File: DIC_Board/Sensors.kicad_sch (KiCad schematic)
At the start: 0 parts

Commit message: Separated the power sheets, did the sensor sheets.
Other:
- added sheet ADMONT K96 (admont_k96.kicad_sch)
- added sheet Licor (Licor.kicad_sch)
- added sheet O2 Sensor (o2_sensor.kicad_sch)
- added sheet RH Sensor (rh_sensor.kicad_sch)
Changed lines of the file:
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@@
 		(title "Sensors")
 	)
+	(sheet
+		(at 55.88 44.45)
+		(size 21.59 24.13)
+		(exclude_from_sim no)
+		(in_bom yes)
+		(on_board yes)
+		(dnp no)
+		(fields_autoplaced yes)
+		(stroke
+			(width 0.1524)
+			(type solid)
+		)
+		(fill
+			(color 0 0 0 0)
+		)
+		(property "Sheetname" "Licor"
+			(at 55.88 43.7384 0)
+			(show_name no)
+			(do_not_autoplace no)
+			(effects
+				(font
+					(size 1.27 1.27)
+				)
+				(justify left bottom)
+			)
+		)
+		(property "Sheetfile" "Licor.kicad_sch"
+			(at 55.88 69.1646 0)
+			(show_name no)
+			(do_not_autoplace no)
+			(effects
+				(font
+					(size 1.27 1.27)
+				)
+				(justify left top)
+			)
+		)
+		(instances
+			(project "DIC_Board"
+				(path "/bb0ef0df-c181-443a-843c-695cd2e0efee/15388a04-aea8-414b-8903-58a719a8054d"
+					(page "13")
+				)
+			)
+		)
+	)
+	(sheet
+		(at 101.6 44.45)
+		(size 30.48 24.13)
+		(exclude_from_sim no)
+		(in_bom yes)
+		(on_board yes)
+		(dnp no)
+		(fields_autoplaced yes)
+		(stroke
+			(width 0.1524)
+			(type solid)
+		)
+		(fill
+			(color 0 0 0 0)
+		)
+		(property "Sheetname" "RH Sensor"
+			(at 101.6 43.7384 0)
+			(show_name no)
+			(do_not_autoplace no)
+			(effects
+				(font
+					(size 1.27 1.27)
+				)
+				(justify left bottom)
+			)
+		)
+		(property "Sheetfile" "rh_sensor.kicad_sch"
+			(at 101.6 69.1646 0)
+			(show_name no)
+			(do_not_autoplace no)
+			(effects
+				(font
+					(size 1.27 1.27)
+				)
+				(justify left top)
+			)
+		)
+		(instances
+			(project "DIC_Board"
+				(path "/bb0ef0df-c181-443a-843c-695cd2e0efee/15388a04-aea8-414b-8903-58a719a8054d"
+					(page "14")
+				)
+			)
+		)
+	)
+	(sheet
+		(at 151.13 44.45)
+		(size 25.4 25.4)
+		(exclude_from_sim no)
+		(in_bom yes)
+		(on_board yes)
+		(dnp no)
+		(fields_autoplaced yes)
+		(stroke
+			(width 0.1524)
+			(type solid)
+		)
+		(fill
+			(color 0 0 0 0)
+		)
+		(property "Sheetname" "O2 Sensor"
+			(at 151.13 43.7384 0)
+			(show_name no)
+			(do_not_autoplace no)
+			(effects
+				(font
+					(size 1.27 1.27)
+				)
+				(justify left bottom)
+			)
+		)
+		(property "Sheetfile" "o2_sensor.kicad_sch"
+			(at 151.13 70.4346 0)
+			(show_name no)
+			(do_not_autoplace no)
+			(effects
+				(font
+					(size 1.27 1.27)
+				)
+				(justify left top)
+			)
+		)
+		(instances
+			(project "DIC_Board"
+				(path "/bb0ef0df-c181-443a-843c-695cd2e0efee/15388a04-aea8-414b-8903-58a719a8054d"
+					(page "15")
+				)
+			)
+		)
+	)
+	(sheet
+		(at 191.77 46.99)
+		(size 26.67 24.13)
+		(exclude_from_sim no)
+		(in_bom yes)
+		(on_board yes)
+		(dnp no)
+		(fields_autoplaced yes)
+		(stroke
+			(width 0.1524)
+			(type solid)
+		)
+		(fill
+			(color 0 0 0 0)
+		)
+		(property "Sheetname" "ADMONT K96"
+			(at 191.77 46.2784 0)
+			(show_name no)
+			(do_not_autoplace no)
+			(effects
+				(font
+					(size 1.27 1.27)
+				)
+				(justify left bottom)
+			)
+		)
+		(property "Sheetfile" "admont_k96.kicad_sch"
+			(at 191.77 71.7046 0)
+			(show_name no)
+			(do_not_autoplace no)
+			(effects
+				(font
+					(size 1.27 1.27)
+				)
+				(justify left top)
+			)
+		)
+		(instances
+			(project "DIC_Board"
+				(path "/bb0ef0df-c181-443a-843c-695cd2e0efee/15388a04-aea8-414b-8903-58a719a8054d"
+					(page "16")
+				)
+			)
+		)
+	)
 )

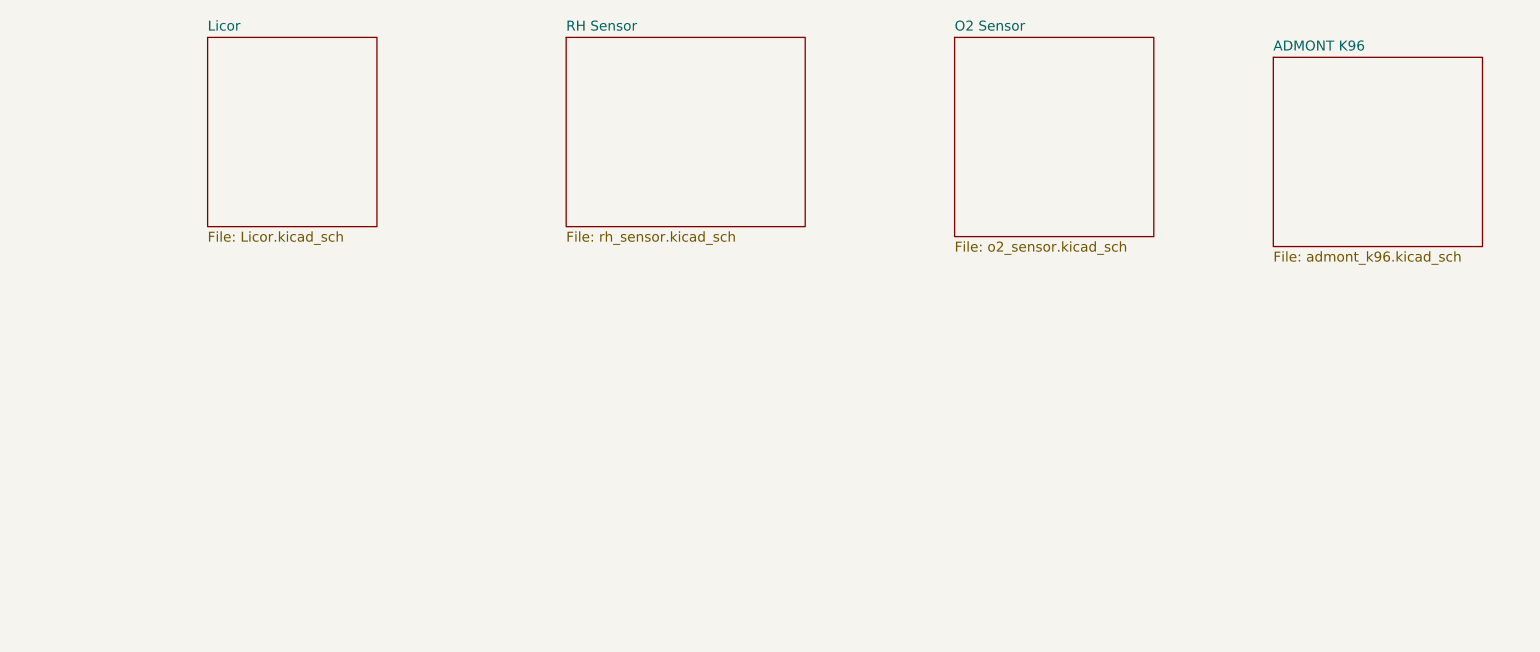
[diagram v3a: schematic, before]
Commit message: Synchronize schematic hierarchy and MCU pin map
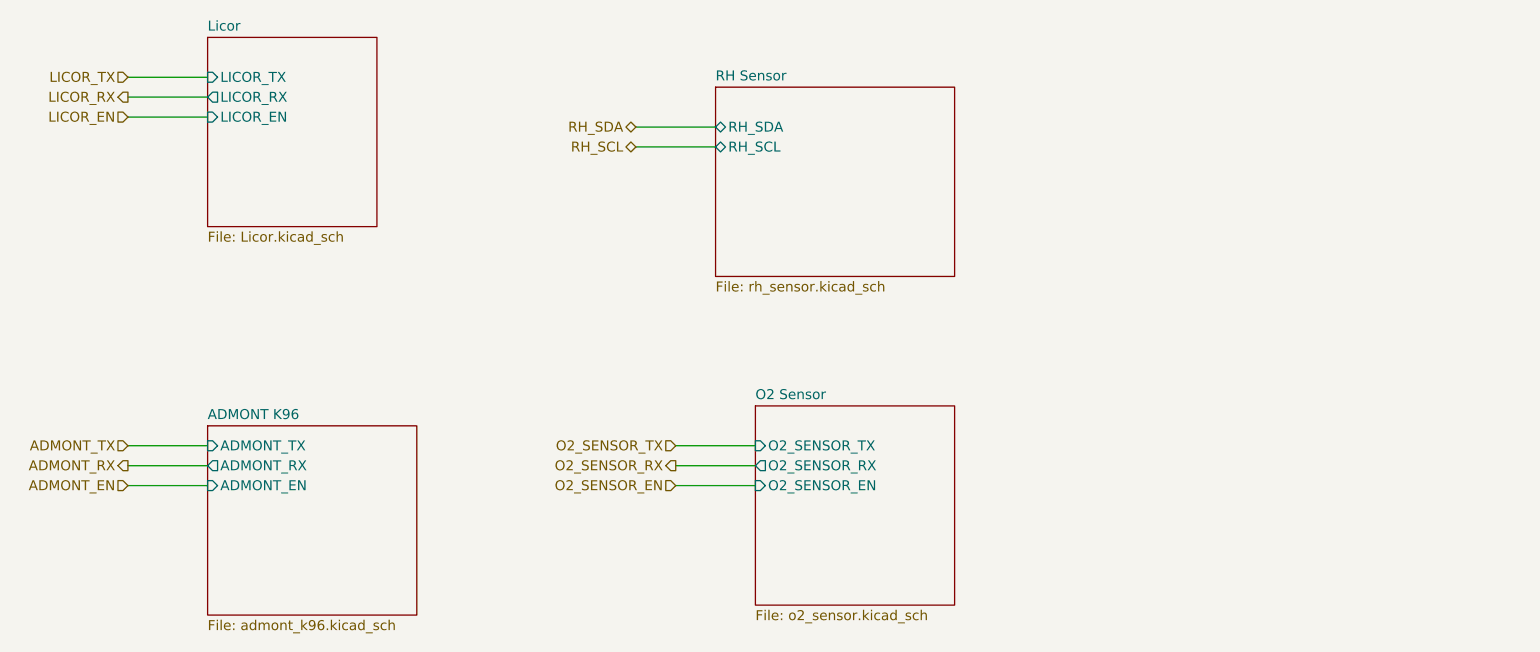
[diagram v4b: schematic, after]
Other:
- sheet ADMONT K96 ports: added ADMONT_EN, ADMONT_RX, ADMONT_TX; removed none
- sheet Licor ports: added LICOR_EN, LICOR_RX, LICOR_TX; removed none
- sheet O2 Sensor ports: added O2_SENSOR_EN, O2_SENSOR_RX, O2_SENSOR_TX; removed none
- sheet RH Sensor ports: added RH_SCL, RH_SDA; removed none
